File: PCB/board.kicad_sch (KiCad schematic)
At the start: 171 parts, among them J1 Micro_SD_Card, J10 Conn_01x10, J11 Conn_01x02, J12 Conn_02x04_Odd_Even, J13 Conn_01x02, J14 Conn_01x02, J15 Conn_01x03, J16 Conn_01x02, J17 Conn_01x05, J18 Conn_01x04, J19 Conn_01x04, J2 Conn_ARM_JTAG_SWD_10, J20 Conn_01x02, J21 Conn_01x03, J22 Conn_02x04_Odd_Even, J23 Conn_01x04, J24 Conn_01x04, J25 Conn_01x02, J26 Conn_01x03, J27 Conn_02x04_Odd_Even, J28 Conn_01x04, J29 Conn_01x04, J30 Conn_01x02, J31 Conn_01x03, J32 Conn_01x02, J33 Conn_01x02, J34 Conn_01x02, J35 Conn_01x02, J36 Conn_01x02, J37 Conn_01x02, J4 Conn_01x04, J5 Conn_01x04, J6 Conn_01x02, J7 Conn_01x03, J8 Conn_02x04_Odd_Even, J9 Conn_01x10, P1 USB_C_Plug_USB2.0, Q1 IRLML6402, Q2 NMOS, Q3 NMOS, Q4 NMOS, Q5 NMOS, Q6 NMOS, SW1 SW_SPST, SW2 SW_Push, U1 STM32H743VITx, U2 AMS1117-3.3, U3 TPS54331, U4 TMC2209_SILENTSTEPSTICK, U5 TMC2209_SILENTSTEPSTICK, U6 TMC2209_SILENTSTEPSTICK, U7 TMC2209_SILENTSTEPSTICK, Y1 25 MHz

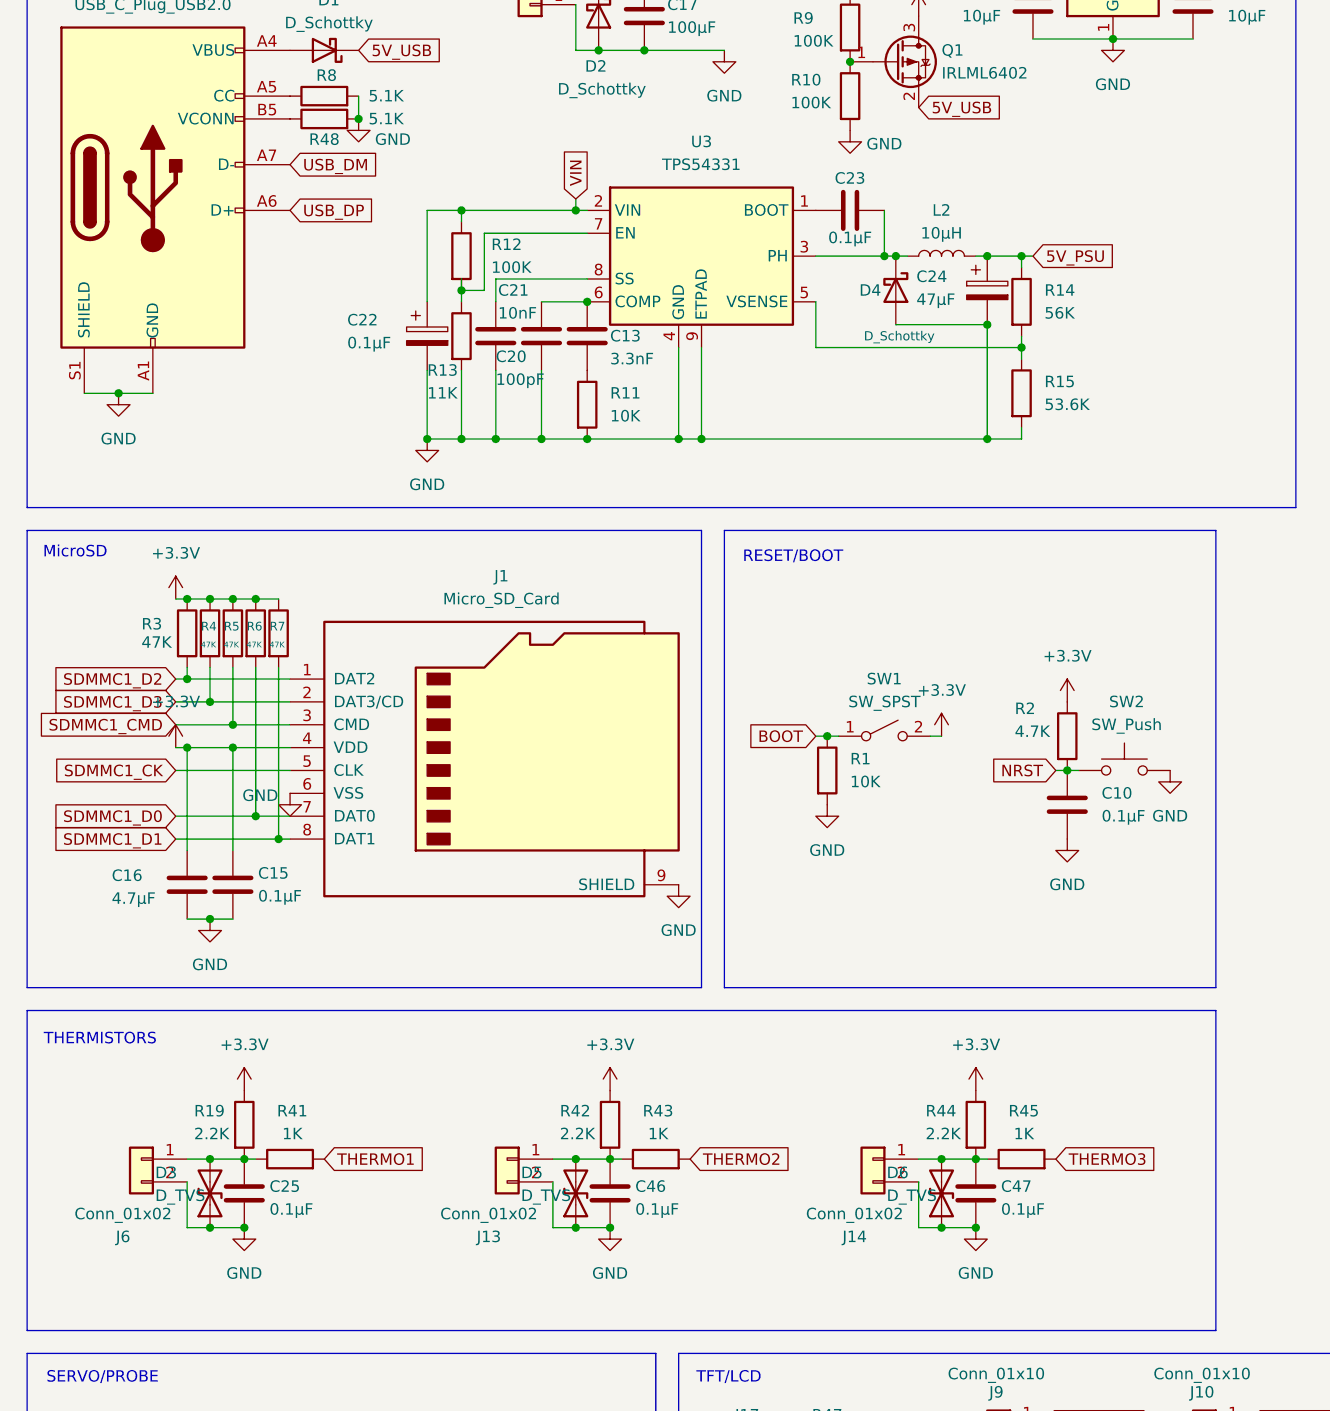
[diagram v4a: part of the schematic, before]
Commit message: added the footprints for the thermistors
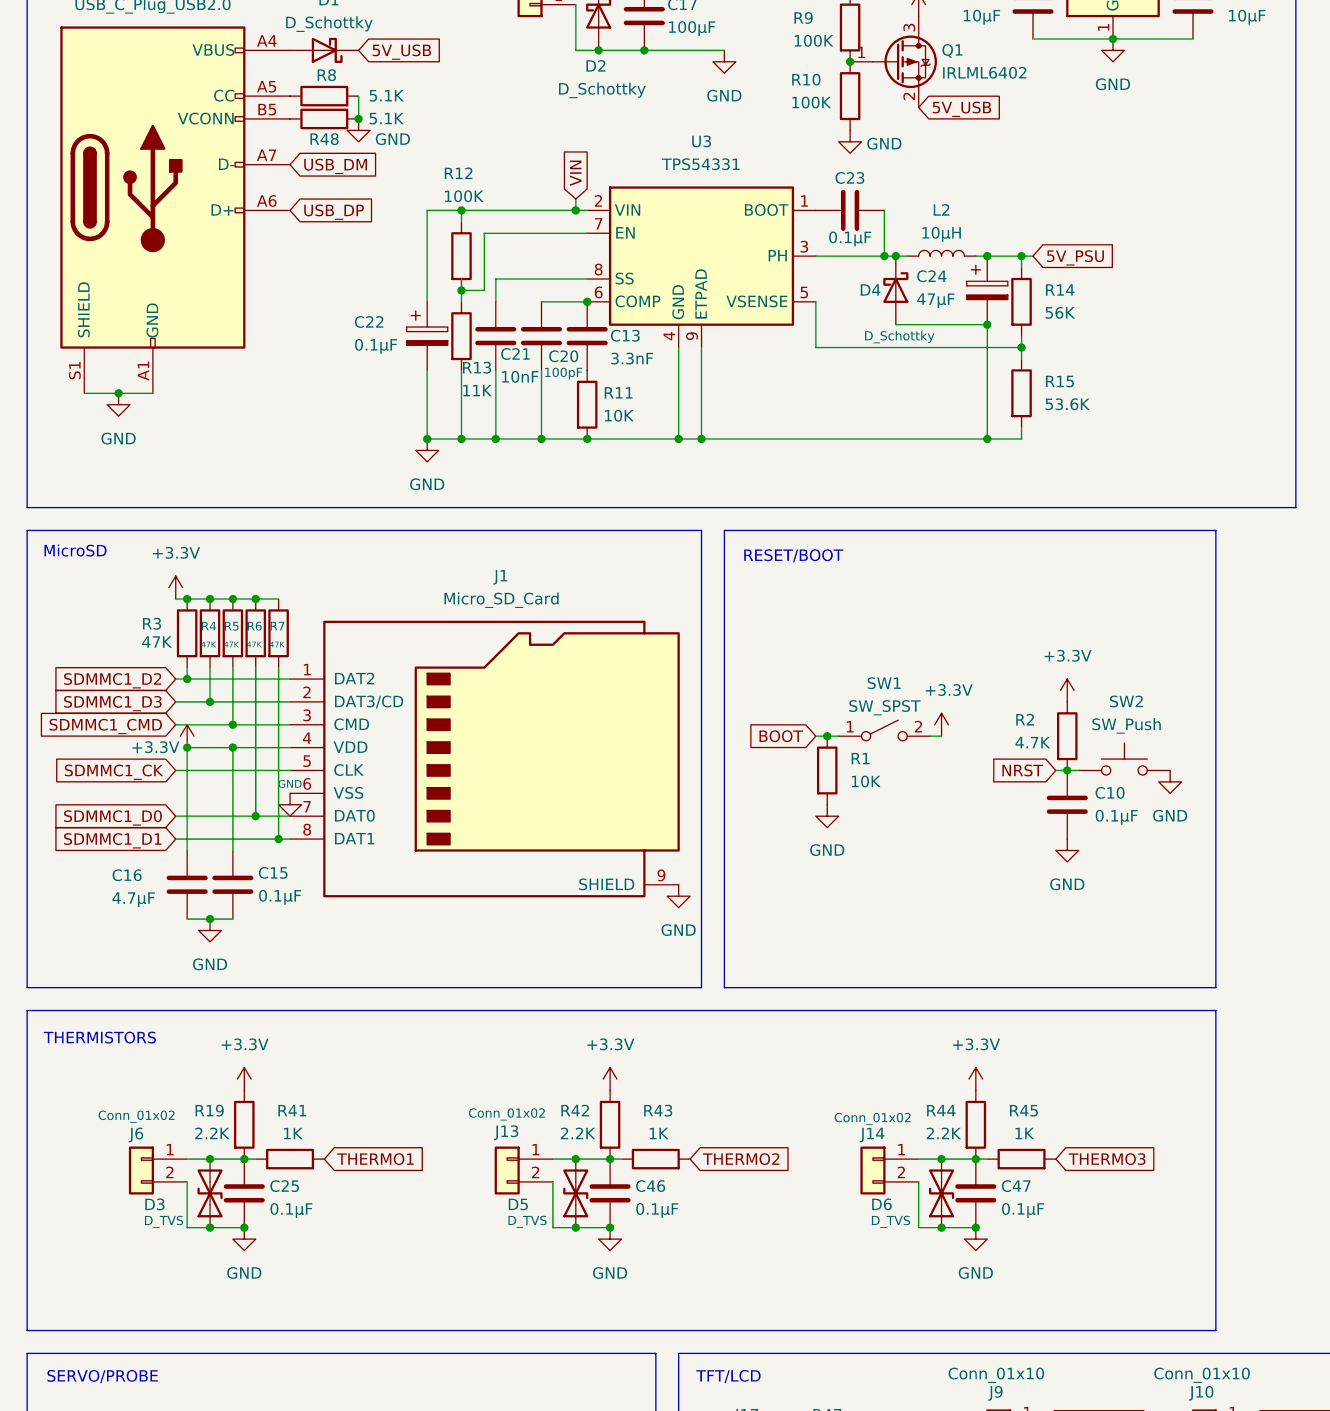
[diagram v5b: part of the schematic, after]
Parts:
- C10, C25, C46, C47: footprint (none) -> Capacitor_SMD:C_0603_1608Metric
- D3, D5, D6: footprint (none) -> Diode_SMD:D_SOD-323
- R1, R19, R2, R41, R42, R43, R44, R45: footprint (none) -> Resistor_SMD:R_0603_1608Metric
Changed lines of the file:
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@@
 	(wire
 		(pts
-			(xy 30.48 109.22) (xy 31.75 109.22)
-		)
-		(stroke
-			(width 0)
-			(type default)
-		)
-	)
-	(wire
-		(pts
 			(xy 214.63 198.12) (xy 215.9 198.12)
 		)
@@
 			)
 		)
-		(property "Footprint" ""
+		(property "Footprint" "Resistor_SMD:R_0603_1608Metric"
 			(at 36.322 151.13 90)
 			(effects
@@
 		(dnp no)
 		(property "Reference" "J14"
-			(at 105.918 163.576 0)
+			(at 107.95 152.146 0)
 			(effects
 				(font
@@
 		)
 		(property "Value" "Conn_01x02"
-			(at 105.918 161.036 0)
+			(at 107.95 150.368 0)
 			(effects
 				(font
-					(size 1.27 1.27)
+					(size 1.016 1.016)
 				)
 			)
@@
 			)
 		)
-		(property "Footprint" ""
+		(property "Footprint" "Resistor_SMD:R_0603_1608Metric"
 			(at 124.46 156.718 90)
 			(effects
@@
 		(dnp no)
 		(property "Reference" "J13"
-			(at 65.278 163.576 0)
+			(at 67.31 151.892 0)
 			(effects
 				(font
@@
 		)
 		(property "Value" "Conn_01x02"
-			(at 65.278 161.036 0)
+			(at 67.31 149.86 0)
 			(effects
 				(font
-					(size 1.27 1.27)
+					(size 1.016 1.016)
 				)
 			)
@@
 		(on_board yes)
 		(dnp no)
-		(fields_autoplaced yes)
 		(property "Reference" "#PWR028"
 			(at 115.57 111.76 0)
@@
 		)
 		(property "Value" "+3.3V"
-			(at 115.57 102.87 0)
+			(at 116.332 102.87 0)
 			(effects
 				(font
@@
 			)
 		)
-		(property "Footprint" ""
+		(property "Footprint" "Resistor_SMD:R_0603_1608Metric"
 			(at 83.82 156.718 90)
 			(effects
@@
 		(dnp no)
 		(property "Reference" "D6"
-			(at 109.474 156.464 90)
+			(at 107.696 160.02 90)
 			(effects
 				(font
@@
 		)
 		(property "Value" "D_TVS"
-			(at 109.474 159.004 90)
+			(at 107.696 161.798 90)
 			(effects
 				(font
-					(size 1.27 1.27)
+					(size 1.016 1.016)
 				)
 				(justify right)
 			)
 		)
-		(property "Footprint" ""
+		(property "Footprint" "Diode_SMD:D_SOD-323"
 			(at 115.57 158.75 0)
 			(effects
@@
 		(dnp no)
 		(property "Reference" "R11"
-			(at 78.74 69.8499 0)
+			(at 77.978 69.85 0)
 			(effects
 				(font
@@
 		)
 		(property "Value" "10K"
-			(at 78.74 72.3899 0)
+			(at 77.978 72.39 0)
 			(effects
 				(font
@@
 		(on_board yes)
 		(dnp no)
-		(fields_autoplaced yes)
 		(property "Reference" "SW1"
-			(at 109.22 101.6 0)
+			(at 109.22 102.108 0)
 			(effects
 				(font
@@
 		)
 		(property "Value" "SW_SPST"
-			(at 109.22 104.14 0)
+			(at 109.22 104.648 0)
 			(effects
 				(font
@@
 		)
 		(property "Value" "GND"
-			(at 39.878 114.554 0)
+			(at 43.18 113.284 0)
 			(effects
 				(font
-					(size 1.27 1.27)
+					(size 0.8636 0.8636)
 				)
 			)
@@
 		(dnp no)
 		(property "Reference" "J6"
-			(at 24.638 163.576 0)
+			(at 26.162 152.146 0)
 			(effects
 				(font
@@
 		)
 		(property "Value" "Conn_01x02"
-			(at 24.638 161.036 0)
+			(at 26.162 150.114 0)
 			(effects
 				(font
-					(size 1.27 1.27)
+					(size 1.016 1.016)
 				)
 			)
@@
 		(dnp no)
 		(property "Reference" "R12"
-			(at 65.532 53.34 0)
+			(at 60.198 45.466 0)
 			(effects
 				(font
@@
 		)
 		(property "Value" "100K"
-			(at 65.532 55.88 0)
+			(at 60.198 48.006 0)
 			(effects
 				(font
@@
 			)
 		)
-		(property "Footprint" ""
+		(property "Footprint" "Resistor_SMD:R_0603_1608Metric"
 			(at 117.602 151.13 90)
 			(effects
@@
 			)
 		)
-		(property "Footprint" ""
+		(property "Footprint" "Resistor_SMD:R_0603_1608Metric"
 			(at 43.18 156.718 90)
 			(effects
@@
 			)
 		)
-		(property "Footprint" ""
+		(property "Footprint" "Resistor_SMD:R_0603_1608Metric"
 			(at 101.092 111.76 90)
 			(effects
@@
 		(dnp no)
 		(property "Reference" "C22"
-			(at 49.53 61.722 0)
+			(at 50.292 61.976 0)
 			(effects
 				(font
@@
 		)
 		(property "Value" "0.1µF"
-			(at 49.53 64.262 0)
+			(at 50.292 64.516 0)
 			(effects
 				(font
@@
 		(dnp no)
 		(property "Reference" "D3"
-			(at 28.194 156.464 90)
+			(at 26.924 160.02 90)
 			(effects
 				(font
@@
 		)
 		(property "Value" "D_TVS"
-			(at 28.194 159.004 90)
+			(at 26.924 161.798 90)
 			(effects
 				(font
-					(size 1.27 1.27)
+					(size 1.016 1.016)
 				)
 				(justify right)
 			)
 		)
-		(property "Footprint" ""
+		(property "Footprint" "Diode_SMD:D_SOD-323"
 			(at 34.29 158.75 0)
 			(effects
@@
 		(dnp no)
 		(property "Reference" "C21"
-			(at 66.294 58.42 0)
+			(at 66.548 65.532 0)
 			(effects
 				(font
@@
 		)
 		(property "Value" "10nF"
-			(at 66.294 60.96 0)
+			(at 66.548 68.072 0)
 			(effects
 				(font
@@
 		(dnp no)
 		(property "Reference" "C20"
-			(at 66.04 65.786 0)
+			(at 71.882 65.786 0)
 			(effects
 				(font
@@
 		)
 		(property "Value" "100pF"
-			(at 66.04 68.326 0)
+			(at 71.374 67.564 0)
 			(effects
 				(font
-					(size 1.27 1.27)
+					(size 1.016 1.016)
 				)
 				(justify left)
@@
 		(dnp no)
 		(property "Reference" "R13"
-			(at 58.42 67.31 0)
+			(at 62.23 67.056 0)
 			(effects
 				(font
@@
 		)
 		(property "Value" "11K"
-			(at 58.42 69.85 0)
+			(at 62.23 69.596 0)
 			(effects
 				(font
@@
 		(on_board yes)
 		(dnp no)
-		(fields_autoplaced yes)
 		(property "Reference" "C10"
-			(at 133.35 114.2999 0)
+			(at 132.588 114.3 0)
 			(effects
 				(font
@@
 		)
 		(property "Value" "0.1µF"
-			(at 133.35 116.8399 0)
+			(at 132.588 116.84 0)
 			(effects
 				(font
@@
 			)
 		)
-		(property "Footprint" ""
+		(property "Footprint" "Capacitor_SMD:C_0603_1608Metric"
 			(at 130.5052 119.38 0)
 			(effects
@@
 		(dnp no)
 		(property "Reference" "D5"
-			(at 68.834 156.464 90)
+			(at 67.31 160.02 90)
 			(effects
 				(font
@@
 		)
 		(property "Value" "D_TVS"
-			(at 68.834 159.004 90)
+			(at 67.31 161.798 90)
 			(effects
 				(font
-					(size 1.27 1.27)
+					(size 1.016 1.016)
 				)
 				(justify right)
 			)
 		)
-		(property "Footprint" ""
+		(property "Footprint" "Diode_SMD:D_SOD-323"
 			(at 74.93 158.75 0)
 			(effects
@@
 		(dnp no)
 		(property "Reference" "R2"
-			(at 123.698 104.902 0)
+			(at 123.698 106.172 0)
 			(effects
 				(font
@@
 		)
 		(property "Value" "4.7K"
-			(at 123.698 107.442 0)
+			(at 123.698 108.712 0)
 			(effects
 				(font
@@
 			)
 		)
-		(property "Footprint" ""
+		(property "Footprint" "Resistor_SMD:R_0603_1608Metric"
 			(at 127.762 107.95 90)
 			(effects
@@
 			)
 		)
-		(property "Footprint" ""
+		(property "Footprint" "Resistor_SMD:R_0603_1608Metric"
 			(at 76.962 151.13 90)
 			(effects
@@
 			)
 		)
-		(property "Footprint" ""
+		(property "Footprint" "Capacitor_SMD:C_0603_1608Metric"
 			(at 120.3452 162.56 0)
 			(effects
@@
 			)
 		)
-		(property "Footprint" ""
+		(property "Footprint" "Capacitor_SMD:C_0603_1608Metric"
 			(at 39.0652 162.56 0)
 			(effects
@@
 			)
 		)
-		(property "Footprint" ""
+		(property "Footprint" "Capacitor_SMD:C_0603_1608Metric"
 			(at 79.7052 162.56 0)
 			(effects
@@
 	(symbol
 		(lib_id "power:+3.3V")
-		(at 30.48 109.22 0)
+		(at 31.75 109.22 0)
 		(unit 1)
 		(exclude_from_sim no)
@@
 		(on_board yes)
 		(dnp no)
-		(fields_autoplaced yes)
 		(property "Reference" "#PWR026"
-			(at 30.48 113.03 0)
+			(at 31.75 113.03 0)
 			(effects
 				(font
@@
 		)
 		(property "Value" "+3.3V"
-			(at 30.48 104.14 0)
+			(at 28.194 109.22 0)
 			(effects
 				(font
@@
 		)
 		(property "Footprint" ""
-			(at 30.48 109.22 0)
+			(at 31.75 109.22 0)
 			(effects
 				(font
@@
 		)
 		(property "Datasheet" ""
-			(at 30.48 109.22 0)
+			(at 31.75 109.22 0)
 			(effects
 				(font
@@
 		)
 		(property "Description" "Power symbol creates a global label with name \"+3.3V\""
-			(at 30.48 109.22 0)
+			(at 31.75 109.22 0)
 			(effects
 				(font
